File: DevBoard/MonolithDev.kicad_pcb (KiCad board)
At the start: 4 copper layers, 196 x 115 mm, 426 parts, among them J101 Pack (welded 4S) - use instea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, J102 Cell 1 NTC 10k 103AT, J103 EV2400 SMBus, J104 Bench PACK_P, J105 Cell 2 NTC 10k 103AT, J106 Cell 3 NTC 10k 103AT, J107 Cell 4 NTC 10k 103AT, J301 SWD, J302 UART debug, J303 Spare GPIO, J401 TYPE-C 16PCB0.8 IP68, J402 I2CC logic analyzer, J501 TYPE-C 16PCB0.8 IP68, J502 I2CC logic analyzer, Q101 AGM404AP1, Q102 AGM404AP1, Q103 AO3400A, Q104 AO3400A, Q401 PGQ04N070, Q402 PGQ04N070, Q403 AO3401A, Q404 AO3401A, Q405 AO3400A, Q406 AO3400A, Q407 PGQ04N070, Q408 PGQ04N070, Q501 PGQ04N070, Q502 PGQ04N070, Q503 AO3401A, Q504 AO3401A, Q505 AO3400A, Q506 AO3400A, Q507 PGQ04N070, Q508 PGQ04N070, SW101 WAKE, SW301 RESET, U101 BQ40Z50RSMR-R2, U102 BQ294700DSGR, U201 INA190A5IDDFR, U202 INA190A1IDDFR, U203 HT7550-1, U204 TPS62177DQCR, U301 STM32WB1MMC, U401 TPS25751DREFR, U402 M24512-DFMC6TG, U403 BQ25756RRVR, U404 TPS62933DRLR, U405 TPD2S300YFFR, U501 TPS25751DREFR, U502 M24512-DFMC6TG, U503 BQ25756RRVR, U504 TPS62933DRLR, U505 TPD2S300YFFR

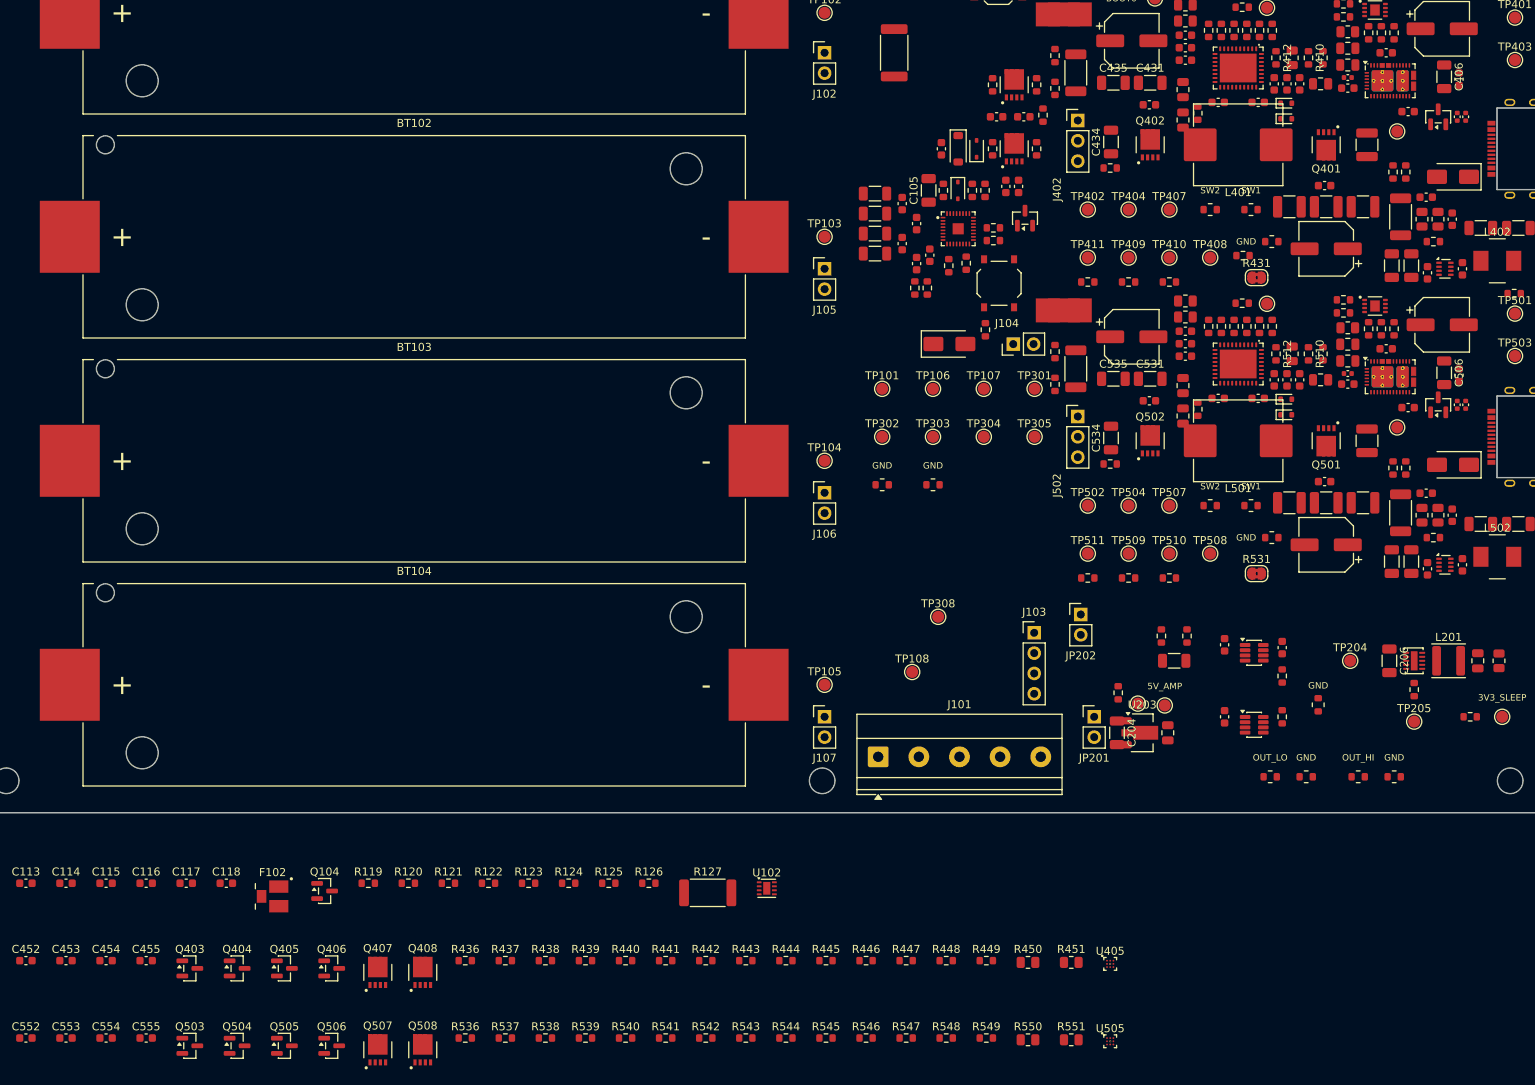
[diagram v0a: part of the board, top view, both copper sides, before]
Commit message: Dev board: 6-layer 1.6 mm board, TPD4S201 port protector, 1.6 mm USB-C
- Stack-up: 6 layers, 1.6 mm, 2 oz outer / 0.5 oz inner (In1/In4 GND),
  0.3 mm drill / 0.45 mm via minimum so JLC's small-via surcharge is gone.
  Via-in-pad (POFV) is free on 6+ layers.
- U405/U505: TPD2S300 (0.4 mm DSBGA) -> TPD4S201TRGRRQ1 (VQFN-20 RGR),
  CC + SBU protection with FLT -> GPIO3. D402/D502 and C453/C553 removed.
- J401/J501: Shou Han TYPE-C 16PCB1.6 IP68 (C55629729), footprint and
  STEP model generated for the 1.6 mm board.
- TPS25751 REF0038A thermal vias 0.2 -> 0.3 mm.
- setup_board.py keeps unmanaged net classes (Kelvin); reset_board.py
  reloads swapped footprints in place.
- ERC 0 errors, DRC schematic parity 0. BOM $77.17 -> $78.65 per board
  at 5 boards.

Co-Authored-By: Claude Opus 5.5 <noreply@anthropic.com>
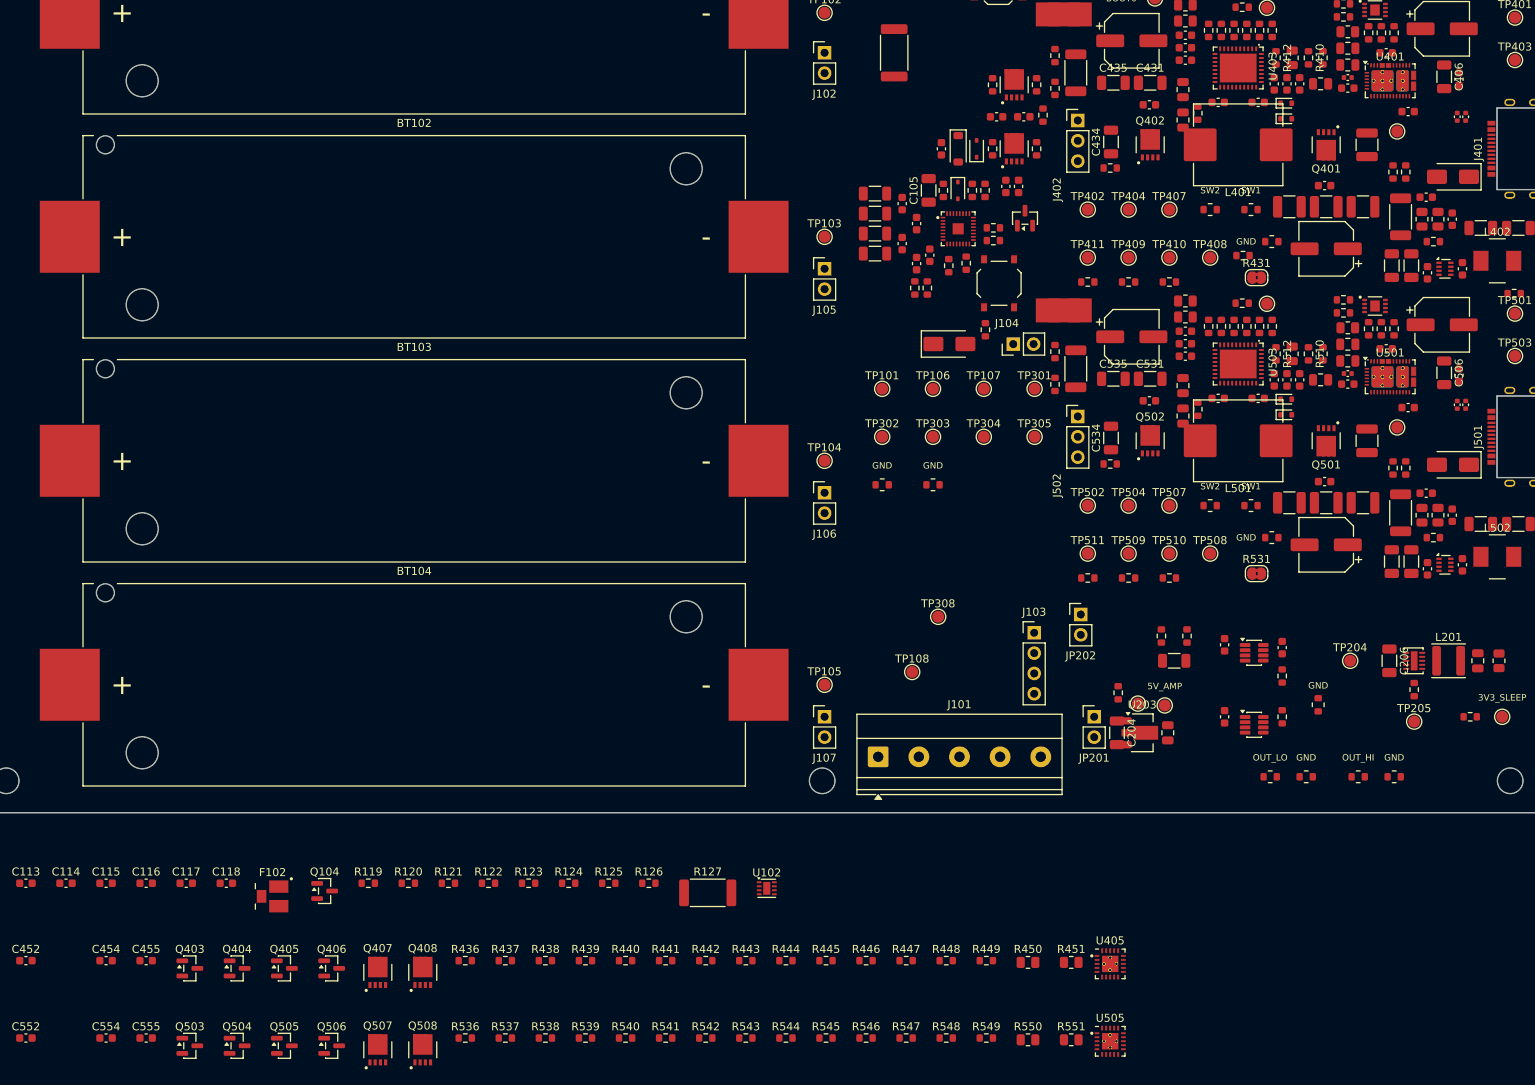
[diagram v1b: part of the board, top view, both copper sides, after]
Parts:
- removed C453, C553: 1u 50V, Capacitor_SMD:C_0603_1608Metric
- removed D402, D502: ESD2CAN24DBZRQ1, Package_TO_SOT_SMD:SOT-23
- J401, J501: value TYPE-C 16PCB0.8 IP68 -> TYPE-C 16PCB1.6 IP68; footprint MonolithDev:USB_C_Receptacle_ShouHan_TYPE-C_16PCB0.8_IP68 -> MonolithDev:USB_C_Receptacle_ShouHan_TYPE-C_16PCB1.6_IP68
- U405, U505: value TPD2S300YFFR -> TPD4S201TRGRRQ1; footprint MonolithDev:TI_YFF0009_DSBGA-9_P0.4mm -> MonolithDev:TI_RGR0020C_VQFN-20-1EP_3.5x3.5mm_P0.5mm_EP2.05mm
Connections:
- J401 pad A5: /USB Port 1/CC1 -> /USB Port 1/C_CC1
- J401 pad B5: /USB Port 1/CC2 -> /USB Port 1/C_CC2
- J501 pad A5: /USB Port 2/CC1 -> /USB Port 2/C_CC1
- J501 pad B5: /USB Port 2/CC2 -> /USB Port 2/C_CC2
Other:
- copper layers 4 -> 6

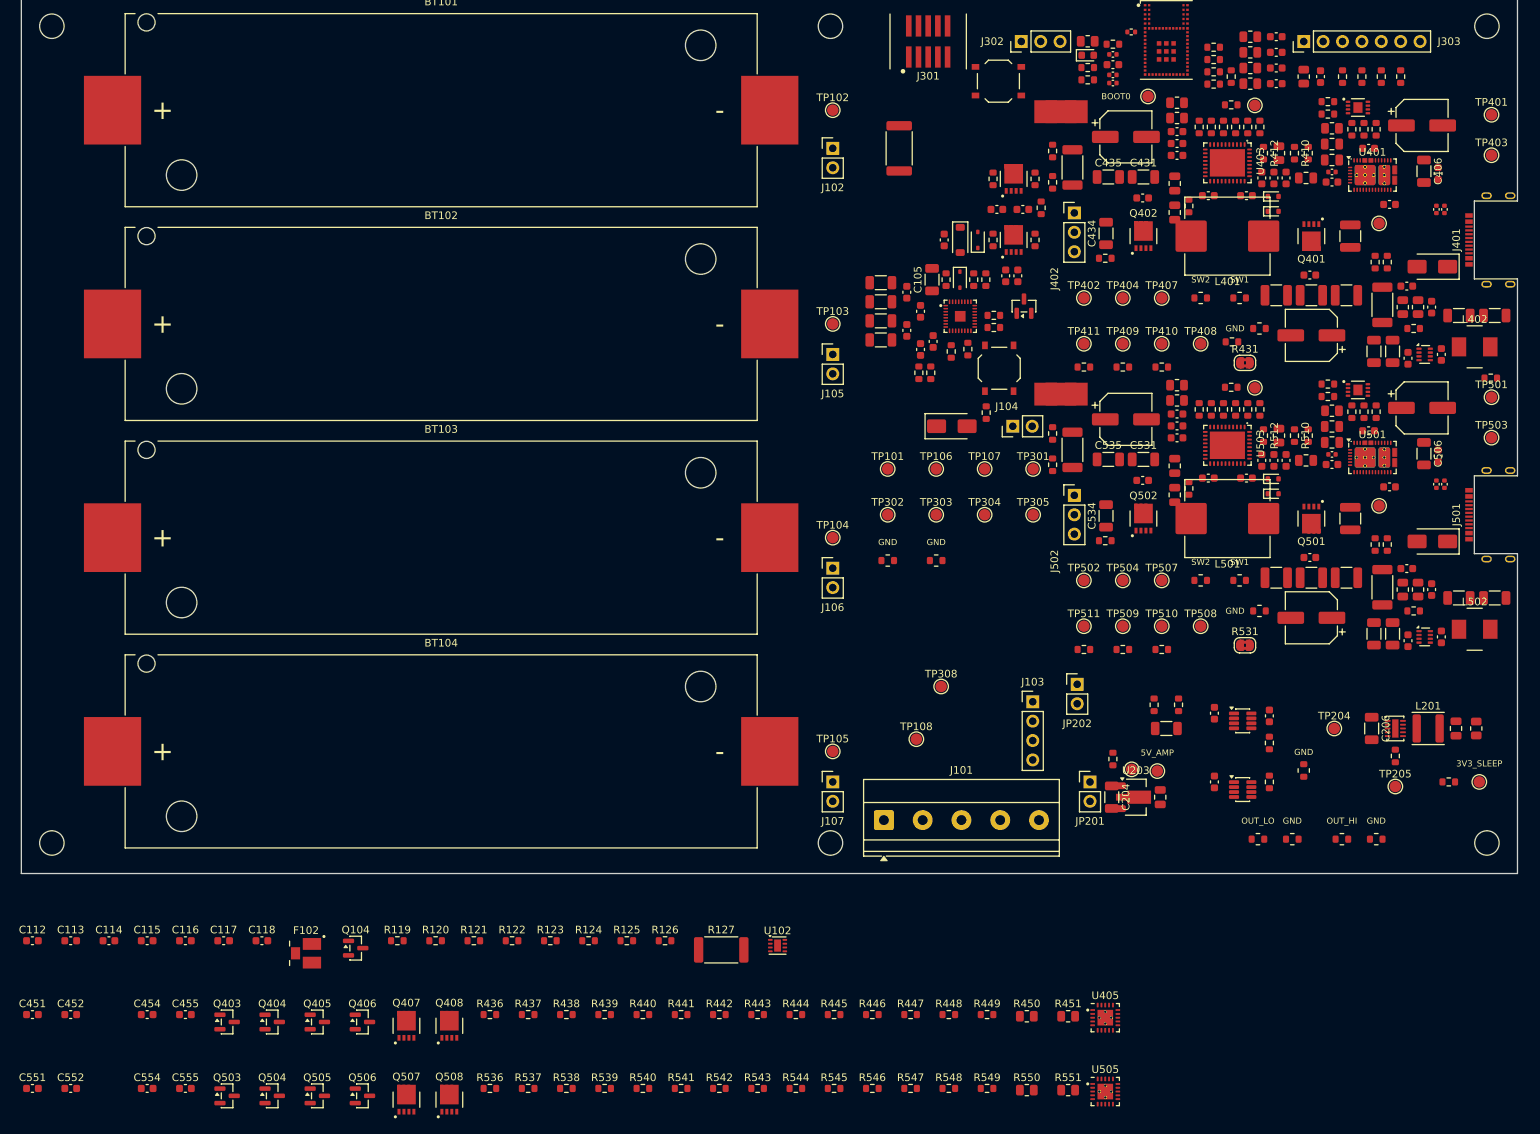
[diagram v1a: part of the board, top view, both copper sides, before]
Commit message: Dev board: block placement, every part in its sheet's zone
New tools/place_blocks.py places all parts on the board, one zone per
schematic page: gauge column, MCU band, two identical 36 mm port bands
(port 2 = port 1 shifted to J501), sleep-current block.

- Port power stage rebuilt for the discrete half-bridges and the
  SMMS1040: vertical FET pairs with their switch nodes facing the
  inductor, C430/C438 straddling HS drain / LS source, MLCC banks on the
  same strips, polymers one step out, gate resistors at the gate pins.
- BQ25756 above the inductor with gate drive facing the stage; TPS25751,
  EEPROM, TPD4S201 and liquid detection toward the connector; PP5V buck
  along the bottom of the band; probe loops and test-pad field.
- BQ294700 second-protector block beside F102 in the gauge column;
  C105 and the HT7550-1 group moved clear.
- No courtyard overlaps, DRC schematic parity 0. No copper or silk pass.

Co-Authored-By: Claude Opus 5.5 <noreply@anthropic.com>
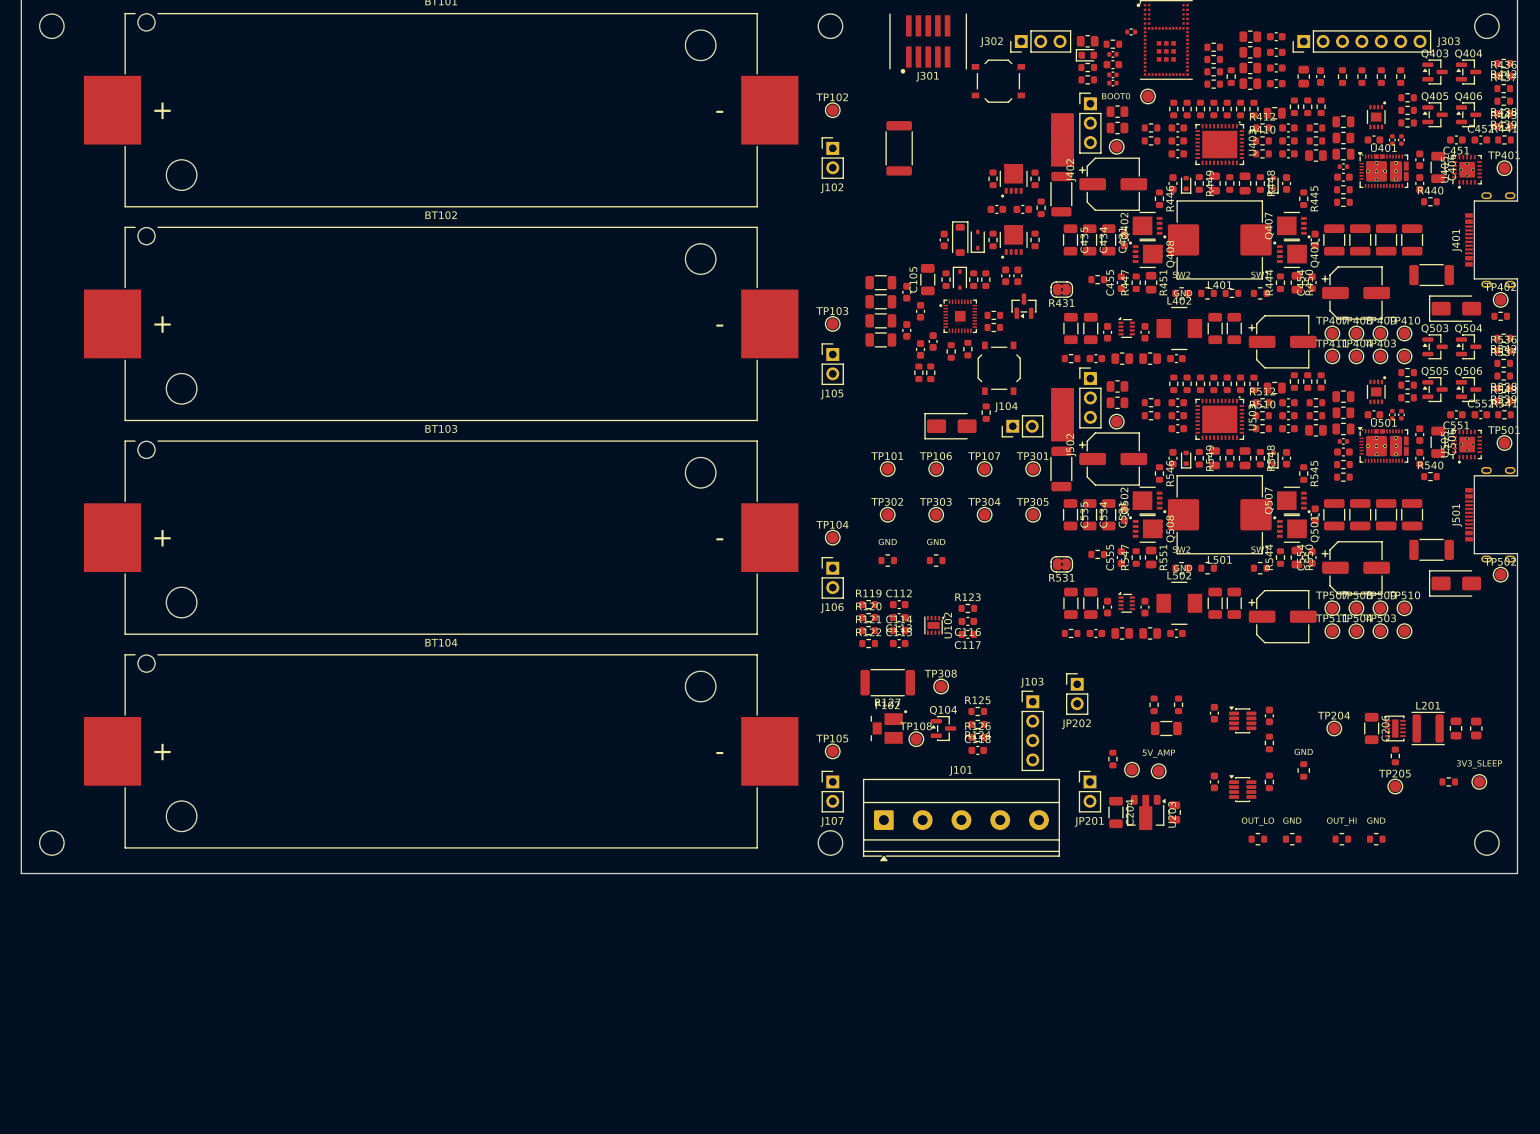
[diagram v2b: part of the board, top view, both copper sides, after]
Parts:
- moved C451 218.9 mm to (238.0, 68.9), turned to 180 degrees
- moved C452 217.4 mm to (241.2, 68.9)
- moved C551 206.4 mm to (238.0, 104.9), turned to 180 degrees
- moved C552 204.7 mm to (241.2, 104.9)
- moved Q403 201.3 mm to (235.2, 60.0)
- moved Q404 200.1 mm to (239.6, 60.0)
- moved Q405 188.6 mm to (235.2, 65.6)
- moved Q406 187.4 mm to (239.6, 65.6)
- moved Q503 186.2 mm to (235.2, 96.0)
- moved Q504 184.9 mm to (239.6, 96.0)
- moved R436 181.0 mm to (244.2, 60.5)
- moved C454 180.2 mm to (219.1, 87.6), turned to 90 degrees
- moved R437 176.2 mm to (244.2, 62.2)
- moved Q505 173.2 mm to (235.2, 101.6)
- moved Q506 171.9 mm to (239.6, 101.6)
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
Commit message: Dev board rev A7 layout: CC2340R5MODA and TMP1075 placed
- Board updated to the rev A7 schematic: U301 CC2340R5MODA at the top edge
  with its RF match, TMP1075 U302-U306 on the copper they measure.
- TMP1075 footprint with 0.3 mm thermal vias (JLC minimum) in place of
  KiCad's 0.2 mm ThermalVias variant.
- DRC 0 errors, schematic parity 0, ERC at the usual 8 warnings.

Co-Authored-By: Claude Opus 5.5 <noreply@anthropic.com>
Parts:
- removed R303: 0R, Resistor_SMD:R_0402_1005Metric
- removed R308, R309, R310, R311, R320: 10k 1%, Resistor_SMD:R_0805_2012Metric
- removed R316: 1k, Resistor_SMD:R_0603_1608Metric
- removed TH301, TH302, TH303, TH304, TH305: 10k B3435, Resistor_SMD:R_0603_1608Metric
- removed TP305: IRQ2, TestPoint:TestPoint_Pad_D1.5mm
- removed TP306: BOOT0, TestPoint:TestPoint_Pad_D1.5mm
- added C313: 15p C0G, Capacitor_SMD:C_0402_1005Metric, F.Cu at (194.8, 53.9)
- added C314: TBD, Capacitor_SMD:C_0402_1005Metric, F.Cu at (192.9, 53.4)
- added C315: 1p C0G, Capacitor_SMD:C_0402_1005Metric, F.Cu at (195.3, 51.4)
- added R321: 0R, Resistor_SMD:R_0402_1005Metric, F.Cu at (194.8, 52.9)
- added U302: TMP1075, MonolithDev:TI_DSG0008A_WSON-8-1EP_2x2mm_P0.5mm_EP0.9x1.6mm_Vias0.3mm, F.Cu at (190.4, 86.4)
- added U303: TMP1075, MonolithDev:TI_DSG0008A_WSON-8-1EP_2x2mm_P0.5mm_EP0.9x1.6mm_Vias0.3mm, F.Cu at (190.4, 122.4)
- added U304: TMP1075, MonolithDev:TI_DSG0008A_WSON-8-1EP_2x2mm_P0.5mm_EP0.9x1.6mm_Vias0.3mm, F.Cu at (243.2, 92.6)
- added U305: TMP1075, MonolithDev:TI_DSG0008A_WSON-8-1EP_2x2mm_P0.5mm_EP0.9x1.6mm_Vias0.3mm, F.Cu at (208.8, 88.8)
- added U306: TMP1075, MonolithDev:TI_DSG0008A_WSON-8-1EP_2x2mm_P0.5mm_EP0.9x1.6mm_Vias0.3mm, F.Cu at (180.0, 78.0)
- C308, C309, C310, C311, C312: footprint Capacitor_SMD:C_0603_1608Metric -> Capacitor_SMD:C_0402_1005Metric
- R302: value 10k -> 100k
- R313: value 100k -> 470k
- TP304: value IRQ1 -> IRQ_N
- U301: value STM32WB1MMC -> CC2340R5MODA; footprint MonolithDev:ST_LGA-77_STM32WB1MMC_6.5x10mm -> MonolithDev:TI_MHA0024A_CC2340R5MODA_7x10mm
- moved C309 68.5 mm to (192.6, 122.4), turned to -90 degrees
- moved C312 45.7 mm to (177.9, 78.0)
- moved C310 45.3 mm to (245.2, 92.6), turned to 90 degrees
- moved C308 37.9 mm to (192.6, 86.4), turned to -90 degrees
- moved C311 29.7 mm to (208.8, 90.7), turned to 180 degrees
- moved C110 5.21 mm to (182.9, 77.2), turned to 0 degrees
- moved C303 4.89 mm to (194.8, 56.9)
- moved C302 4.84 mm to (194.8, 55.9)
- moved C304 3.96 mm to (194.8, 61.2)
- moved R302 3.75 mm to (194.3, 59.9), turned to 0 degrees
- moved C111 1.92 mm to (182.9, 78.8), turned to 180 degrees
- moved C301 1.56 mm to (194.3, 58.2)
- moved U301 0.50 mm to (200.0, 55.3)
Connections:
- C308 pad 1: /MCU and NTCs/NTC_TH1 -> 3V3
- C309 pad 1: /MCU and NTCs/NTC_TH2 -> 3V3
- C310 pad 1: /MCU and NTCs/NTC_TH3 -> 3V3
- C311 pad 1: /MCU and NTCs/NTC_TH4 -> 3V3
- C312 pad 1: /MCU and NTCs/NTC_TH5 -> 3V3
- J303 pad 2: /MCU and NTCs/NTC_TH5 -> IRQ_N
- J303 pad 3: /MCU and NTCs/J303_NTC_EN -> unconnected-(J303-Pin_3-Pad3)
- Q103 pad 3: GAUGE_BTP -> IRQ_N
- R114 pad 2: GAUGE_BTP -> IRQ_N
- R302 pad 1: Net-(U301-BOOT0) -> /MCU and NTCs/3V3_MCU
- R302 pad 2: GND -> /MCU and NTCs/NRST
- R314 pad 2: IRQ1 -> IRQ_N
- R315 pad 2: IRQ2 -> IRQ_N
- TP107 pad 1: GAUGE_BTP -> IRQ_N
- TP304 pad 1: IRQ1 -> IRQ_N
- U301 pad 10: /MCU and NTCs/NTC_EN -> SDA
- U301 pad 11: /MCU and NTCs/NTC_TH1 -> CHG_INH
- U301 pad 12: GAUGE_BTP -> EN_5V1
- U301 pad 13: IRQ2 -> EN_5V2
- U301 pad 14: CHG_INH -> /MCU and NTCs/NRST
- U301 pad 15: GND -> 3V3_SLEEP
- U301 pad 16: /MCU and NTCs/3V3_MCU -> /MCU and NTCs/UART_TX
- U301 pad 17: GND -> /MCU and NTCs/UART_RX
- U301 pad 18: /MCU and NTCs/3V3_MCU -> /MCU and NTCs/LED_DRV
- U301 pad 19: GND -> Net-(J301-Pin_4)
- U301 pad 20: /MCU and NTCs/3V3_MCU -> Net-(J301-Pin_2)
- U301 pad 21: GND -> IRQ_N
- U301 pad 22: Net-(U301-BOOT0) -> GND
- U301 pad 23: /MCU and NTCs/NRST -> GND
- U301 pad 3: GND -> /MCU and NTCs/ANT_IN
- U301 pad 4: GND -> /MCU and NTCs/RFIO
- U301 pad 6: Net-(U301-ANT_IN) -> /MCU and NTCs/3V3_MCU
- U301 pad 7: Net-(U301-ANT_OUT) -> /MCU and NTCs/3V3_MCU
- U301 pad 9: /MCU and NTCs/NTC_TH3 -> SCL
- U401 pad 10: IRQ1 -> IRQ_N
- U501 pad 10: IRQ2 -> IRQ_N
